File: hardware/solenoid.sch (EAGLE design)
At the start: 32 parts, among them U2 AP2204R

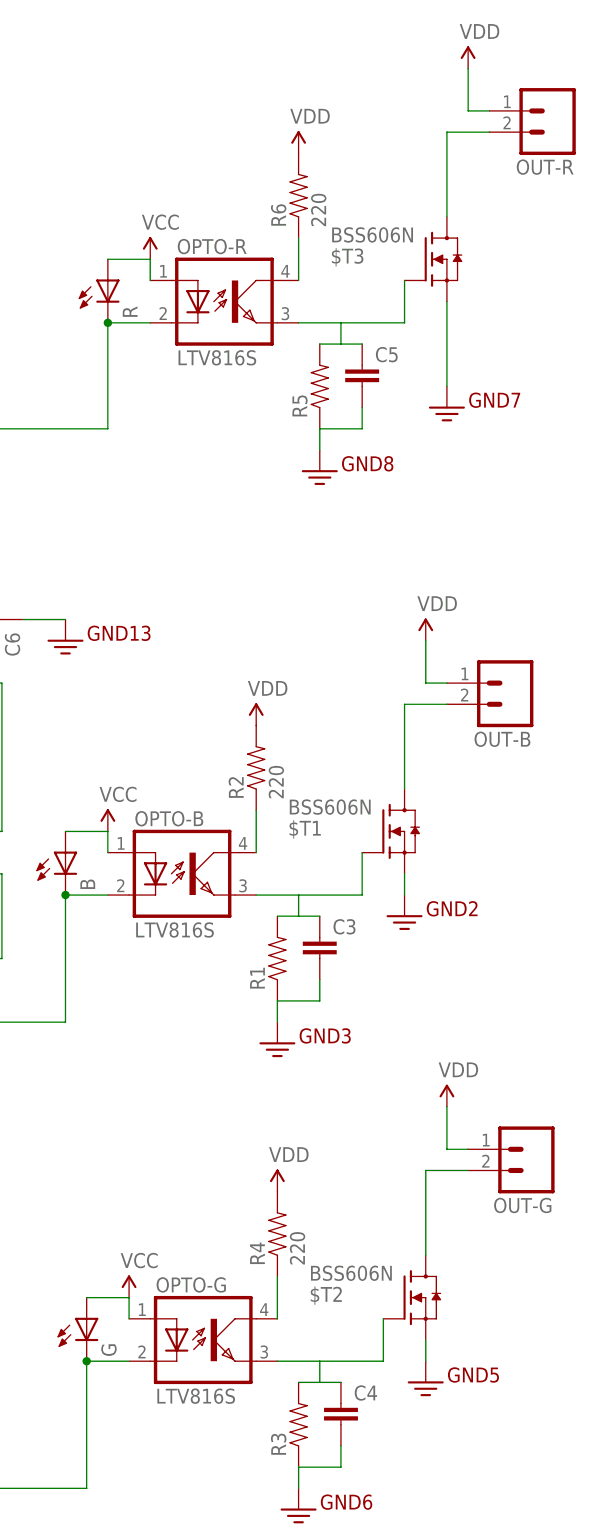
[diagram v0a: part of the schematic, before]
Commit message: Added protection diodes
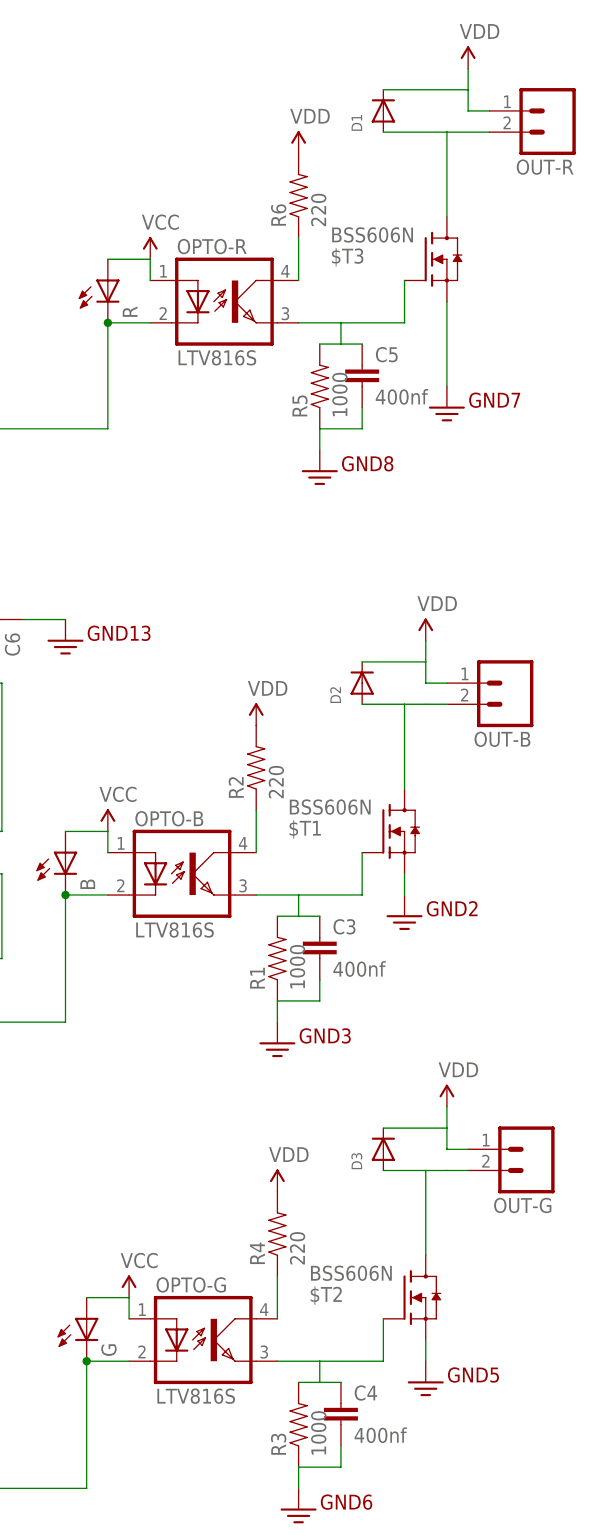
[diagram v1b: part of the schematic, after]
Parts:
- added D1, D2, D3: (no value), microbuilder:DIODESOD-123
- C3, C4, C5: value (none) -> 400nf
- R1, R3, R5: value (none) -> 1000
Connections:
- net N$12: now also D1.A
- net N$4: now also D2.A
- net N$8: now also D3.A
- net VDD: now also D1.C, D2.C, D3.C
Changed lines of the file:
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@@
 <part name="$T1" library="mishafarms" deviceset="BSS606N" device=""/>
 <part name="OPTO-B" library="optocoupler" deviceset="LTV816" device="S"/>
-<part name="R1" library="SparkFun-Passives" deviceset="RESISTOR" device="0805-RES"/>
+<part name="R1" library="SparkFun-Passives" deviceset="RESISTOR" device="0805-RES" value="1000"/>
 <part name="R2" library="SparkFun-Passives" deviceset="RESISTOR" device="0805-RES" value="220"/>
 <part name="GND1" library="SparkFun-Aesthetics" deviceset="GND2" device=""/>
@@
 <part name="C1" library="SparkFun-Capacitors" deviceset="CAP" device="0805" value="1uf"/>
 <part name="C2" library="SparkFun-Capacitors" deviceset="CAP" device="0805" value="2.2uf"/>
-<part name="C3" library="SparkFun-Capacitors" deviceset="CAP" device="0805"/>
+<part name="C3" library="SparkFun-Capacitors" deviceset="CAP" device="0805" value="400nf"/>
 <part name="$T2" library="mishafarms" deviceset="BSS606N" device=""/>
 <part name="OPTO-G" library="optocoupler" deviceset="LTV816" device="S"/>
-<part name="R3" library="SparkFun-Passives" deviceset="RESISTOR" device="0805-RES"/>
+<part name="R3" library="SparkFun-Passives" deviceset="RESISTOR" device="0805-RES" value="1000"/>
 <part name="R4" library="SparkFun-Passives" deviceset="RESISTOR" device="0805-RES" value="220"/>
 <part name="GND5" library="SparkFun-Aesthetics" deviceset="GND2" device=""/>
@@
 <part name="G" library="led" deviceset="LED" device="CHIPLED_0805"/>
 <part name="OUT-G" library="SparkFun-Connectors" deviceset="M02" device="PTH"/>
-<part name="C4" library="SparkFun-Capacitors" deviceset="CAP" device="0805"/>
+<part name="C4" library="SparkFun-Capacitors" deviceset="CAP" device="0805" value="400nf"/>
 <part name="$T3" library="mishafarms" deviceset="BSS606N" device=""/>
 <part name="OPTO-R" library="optocoupler" deviceset="LTV816" device="S"/>
-<part name="R5" library="SparkFun-Passives" deviceset="RESISTOR" device="0805-RES"/>
+<part name="R5" library="SparkFun-Passives" deviceset="RESISTOR" device="0805-RES" value="1000"/>
 <part name="R6" library="SparkFun-Passives" deviceset="RESISTOR" device="0805-RES" value="220"/>
 <part name="GND7" library="SparkFun-Aesthetics" deviceset="GND2" device=""/>
@@
 <part name="R" library="led" deviceset="LED" device="CHIPLED_0805"/>
 <part name="OUT-R" library="SparkFun-Connectors" deviceset="M02" device="PTH"/>
-<part name="C5" library="SparkFun-Capacitors" deviceset="CAP" device="0805"/>
+<part name="C5" library="SparkFun-Capacitors" deviceset="CAP" device="0805" value="400nf"/>
 <part name="IN" library="SparkFun-Connectors" deviceset="M03" device="1X03_NO_SILK"/>
 <part name="OUT" library="SparkFun-Connectors" deviceset="M03" device="1X03_NO_SILK"/>
@@
 <part name="GND13" library="SparkFun-Aesthetics" deviceset="GND2" device=""/>
 <part name="R8" library="SparkFun-Passives" deviceset="RESISTOR" device="0805-RES" value="100"/>
+<part name="D1" library="microbuilder" deviceset="DIODE" device="SOD-123"/>
+<part name="D2" library="microbuilder" deviceset="DIODE" device="SOD-123"/>
+<part name="D3" library="microbuilder" deviceset="DIODE" device="SOD-123"/>
 </parts>
 <sheets>
@@
 <instance part="GND13" gate="G$1" x="91.44" y="121.92"/>
 <instance part="R8" gate="G$1" x="78.74" y="132.08" rot="R270"/>
+<instance part="D1" gate="G$1" x="129.54" y="185.42" rot="R90"/>
+<instance part="D2" gate="G$1" x="127" y="116.84" rot="R90"/>
+<instance part="D3" gate="G$1" x="129.54" y="60.96" rot="R90"/>
 </instances>
 <busses>
@@
 <segment>
 <pinref part="SUPPLY3" gate="VDD" pin="VDD"/>
-<wire x1="134.62" y1="121.92" x2="134.62" y2="116.84" width="0.1524" layer="91"/>
+<wire x1="134.62" y1="121.92" x2="134.62" y2="119.38" width="0.1524" layer="91"/>
 <pinref part="OUT-B" gate="G$1" pin="1"/>
+<wire x1="134.62" y1="119.38" x2="134.62" y2="116.84" width="0.1524" layer="91"/>
 <wire x1="134.62" y1="116.84" x2="137.16" y2="116.84" width="0.1524" layer="91"/>
+<pinref part="D2" gate="G$1" pin="C"/>
+<wire x1="127" y1="119.38" x2="134.62" y2="119.38" width="0.1524" layer="91"/>
 </segment>
 <segment>
@@
 <segment>
 <pinref part="SUPPLY9" gate="VDD" pin="VDD"/>
-<wire x1="137.16" y1="66.04" x2="137.16" y2="60.96" width="0.1524" layer="91"/>
+<wire x1="137.16" y1="66.04" x2="137.16" y2="63.5" width="0.1524" layer="91"/>
 <pinref part="OUT-G" gate="G$1" pin="1"/>
+<wire x1="137.16" y1="63.5" x2="137.16" y2="60.96" width="0.1524" layer="91"/>
 <wire x1="137.16" y1="60.96" x2="139.7" y2="60.96" width="0.1524" layer="91"/>
+<pinref part="D3" gate="G$1" pin="C"/>
+<wire x1="129.54" y1="63.5" x2="137.16" y2="63.5" width="0.1524" layer="91"/>
 </segment>
 <segment>
@@
 <segment>
 <pinref part="SUPPLY12" gate="VDD" pin="VDD"/>
-<wire x1="139.7" y1="190.5" x2="139.7" y2="185.42" width="0.1524" layer="91"/>
+<wire x1="139.7" y1="190.5" x2="139.7" y2="187.96" width="0.1524" layer="91"/>
 <pinref part="OUT-R" gate="G$1" pin="1"/>
+<wire x1="139.7" y1="187.96" x2="139.7" y2="185.42" width="0.1524" layer="91"/>
 <wire x1="139.7" y1="185.42" x2="142.24" y2="185.42" width="0.1524" layer="91"/>
+<pinref part="D1" gate="G$1" pin="C"/>
+<wire x1="129.54" y1="187.96" x2="139.7" y2="187.96" width="0.1524" layer="91"/>
 </segment>
 <segment>
@@
 <segment>
 <pinref part="OUT-B" gate="G$1" pin="2"/>
-<wire x1="137.16" y1="114.3" x2="132.08" y2="114.3" width="0.1524" layer="91"/>
+<wire x1="137.16" y1="114.3" x2="134.62" y2="114.3" width="0.1524" layer="91"/>
 <pinref part="$T1" gate="G$1" pin="D"/>
+<wire x1="134.62" y1="114.3" x2="132.08" y2="114.3" width="0.1524" layer="91"/>
 <wire x1="132.08" y1="114.3" x2="132.08" y2="104.14" width="0.1524" layer="91"/>
+<pinref part="D2" gate="G$1" pin="A"/>
+<wire x1="127" y1="114.3" x2="132.08" y2="114.3" width="0.1524" layer="91"/>
 </segment>
 </net>
@@
 <segment>
 <pinref part="OUT-G" gate="G$1" pin="2"/>
-<wire x1="139.7" y1="58.42" x2="134.62" y2="58.42" width="0.1524" layer="91"/>
+<wire x1="139.7" y1="58.42" x2="137.16" y2="58.42" width="0.1524" layer="91"/>
 <pinref part="$T2" gate="G$1" pin="D"/>
+<wire x1="137.16" y1="58.42" x2="134.62" y2="58.42" width="0.1524" layer="91"/>
 <wire x1="134.62" y1="58.42" x2="134.62" y2="48.26" width="0.1524" layer="91"/>
+<pinref part="D3" gate="G$1" pin="A"/>
+<wire x1="129.54" y1="58.42" x2="134.62" y2="58.42" width="0.1524" layer="91"/>
 </segment>
 </net>
@@
 <pinref part="$T3" gate="G$1" pin="D"/>
 <wire x1="137.16" y1="182.88" x2="137.16" y2="172.72" width="0.1524" layer="91"/>
-</segment>
-</net>
+<pinref part="D1" gate="G$1" pin="A"/>
+<wire x1="129.54" y1="182.88" x2="137.16" y2="182.88" width="0.1524" layer="91"/>
+</segment>
+</net>

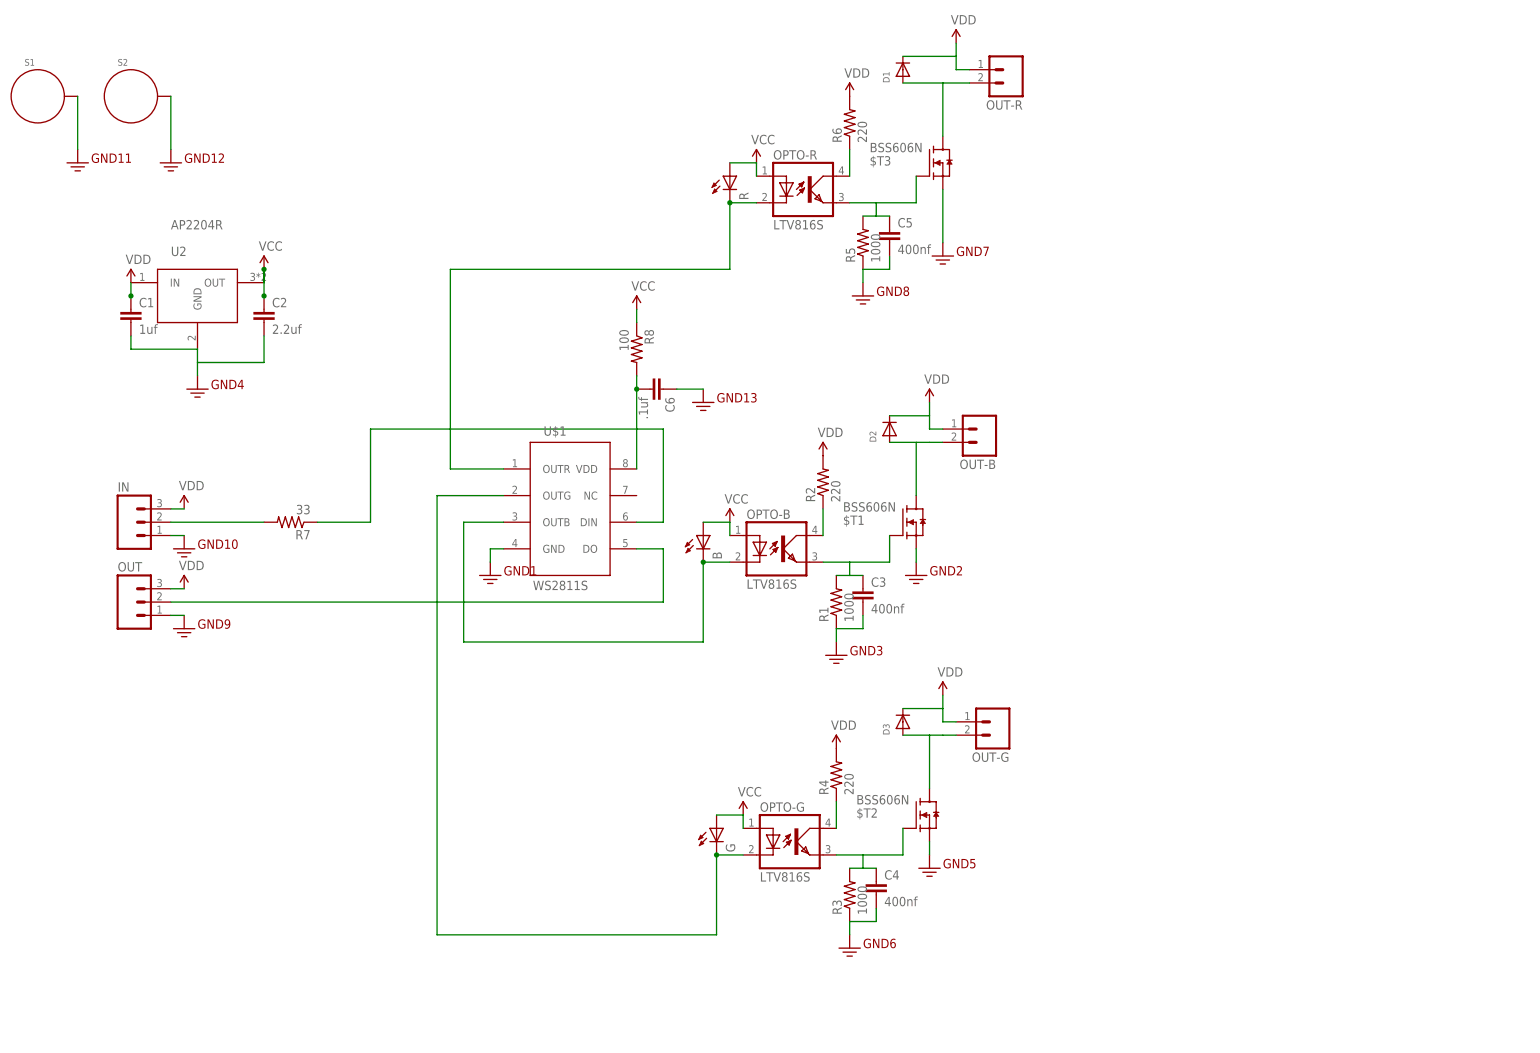
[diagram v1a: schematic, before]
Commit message: Changed to TSDs instead of flyback diodes and increased the solder holw sizes
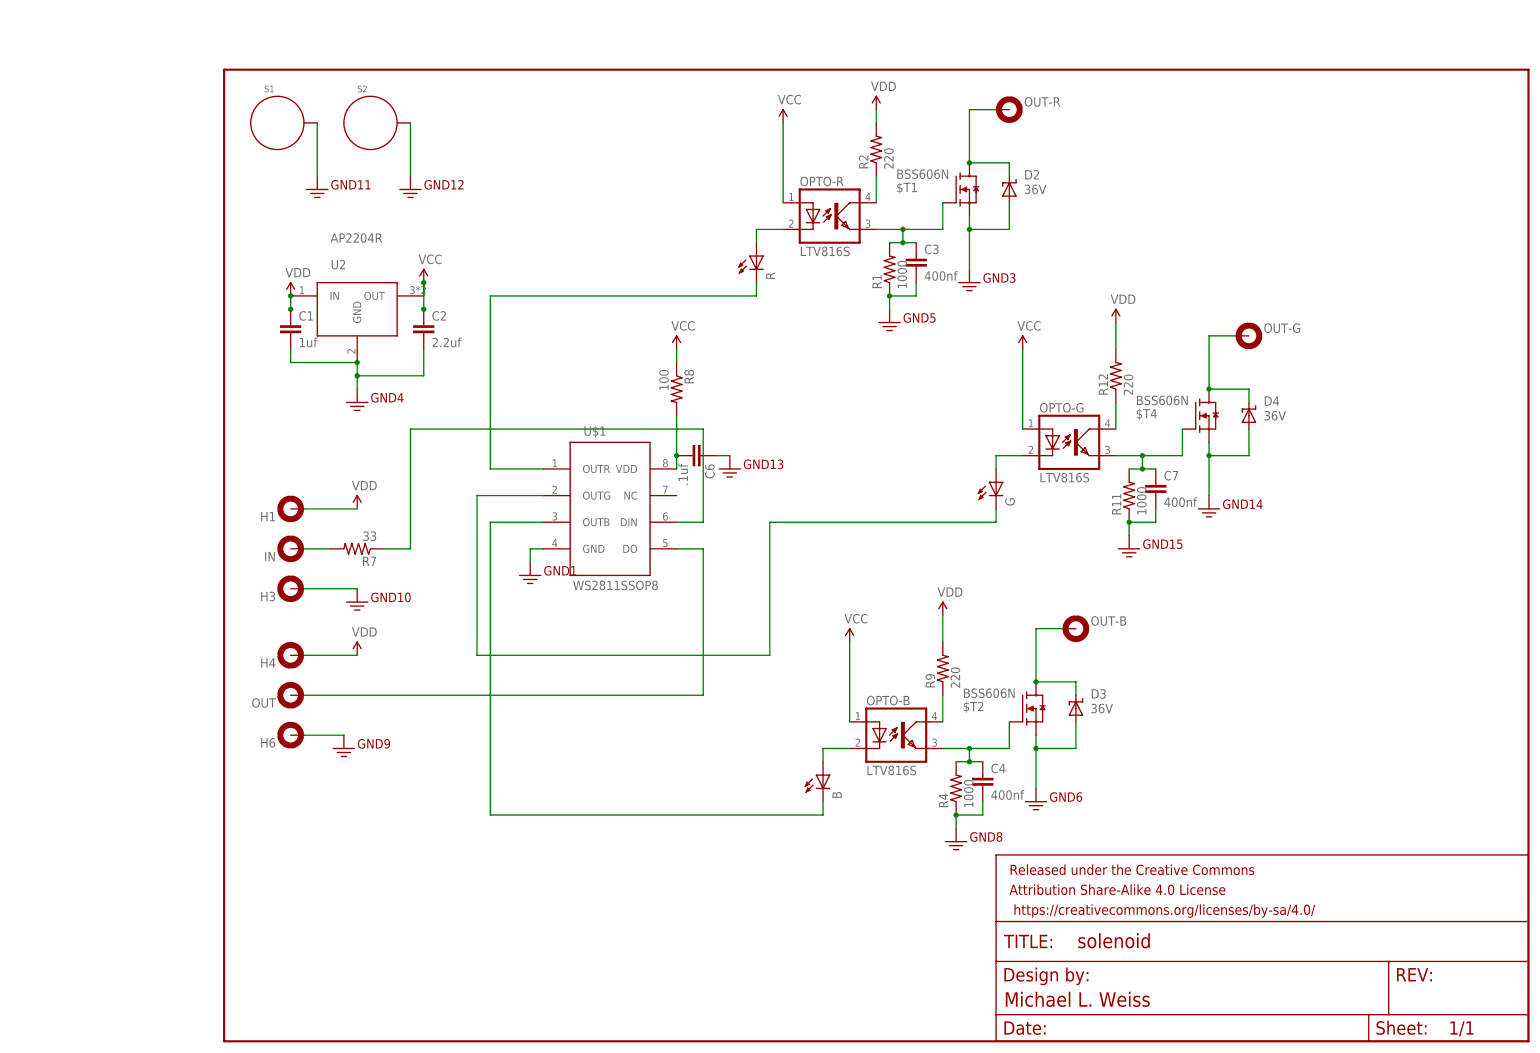
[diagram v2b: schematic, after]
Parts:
- removed $T3: BSS606N, mishafarms:BSS606N
- removed C5: 400nf, SparkFun-Capacitors:CAP0805
- removed D1: (no value), microbuilder:DIODESOD-123
- removed R3, R5: 1000, SparkFun-Passives:RESISTOR0805-RES
- removed R6: 220, SparkFun-Passives:RESISTOR0805-RES
- added $T4: BSS606N, mishafarms:BSS606N
- added C7: 400nf, SparkFun-Capacitors:CAP0805
- added D4: 36V, mishafarms:SUPPRESSOR-SMBJ
- added FRAME1: FRAME-LETTERNO_PACKAGE, SparkFun-Aesthetics:FRAME-LETTERNO_PACKAGE
- added H1, H3, H4, H6: MOUNT-PAD-ROUND2.8, holes:MOUNT-PAD-ROUND2.8
- added R11: 1000, SparkFun-Passives:RESISTOR0805-RES
- added R12, R9: 220, SparkFun-Passives:RESISTOR0805-RES
- D2, D3: value (none) -> 36V; device microbuilder:DIODESOD-123 -> mishafarms:SUPPRESSOR-SMBJ
- IN, OUT: value (none) -> MOUNT-PAD-ROUND2.8; device SparkFun-Connectors:M031X03_NO_SILK -> holes:MOUNT-PAD-ROUND2.8
- OUT-B, OUT-G, OUT-R: value (none) -> MOUNT-PAD-ROUND2.8; device SparkFun-Connectors:M02PTH -> holes:MOUNT-PAD-ROUND2.8
- R4: value 220 -> 1000
- U$1: value WS2811S -> WS2811SSOP8; device mishafarms:WS2811S -> mishafarms:WS2811SSOP8
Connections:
- removed net N$10: $T3.G, C5.1, OPTO-R.EMIT, R5.2
- removed net N$11: OPTO-R.COL, R6.1
- removed net N$14: OUT.2, U$1.DO
- removed net N$2: $T1.G, C3.1, OPTO-B.EMIT, R1.2
- removed net N$3: OPTO-B.COL, R2.1
- removed net N$30: IN.2, R7.2
- removed net N$4: $T1.D, D2.A, OUT-B.2
- new net IN: IN.MOUNT, R7.2
- new net N$15: OPTO-B.COL, R9.1
- new net N$16: B.A, OPTO-B.C
- new net N$19: $T4.G, C7.1, OPTO-G.EMIT, R11.2
- new net N$20: OPTO-G.COL, R12.1
- new net N$21: G.A, OPTO-G.C
- new net OUT: OUT.MOUNT, U$1.DO
- new net OUT-B: $T2.D, D3.C, OUT-B.MOUNT
- new net OUT-G: $T4.D, D4.C, OUT-G.MOUNT
- new net OUT-R: $T1.D, D2.C, OUT-R.MOUNT
- net GND: now also $T4.S, C7.2, D2.A, D3.A, D4.A, H3.MOUNT, H6.MOUNT, R11.1, R4.1; no longer $T3.S, C5.2, IN.1, OUT.1, R3.1, R5.1
- net N$1: no longer OPTO-B.C
- net N$12: now also $T2.G, C4.1, OPTO-B.EMIT, R4.2; no longer $T3.D, D1.A, OUT-R.2
- net N$5: no longer OPTO-G.C
- net N$6: now also $T1.G, C3.1, OPTO-R.EMIT, R1.2; no longer $T2.G, C4.1, OPTO-G.EMIT, R3.2
- net N$7: now also OPTO-R.COL, R2.1; no longer OPTO-G.COL, R4.1
- net N$8: now also OPTO-R.C, R.A; no longer $T2.D, D3.A, OUT-G.2
- net N$9: no longer OPTO-R.C
- net VCC: no longer B.A, G.A, R.A
- net VDD: now also H1.MOUNT, H4.MOUNT, R12.2, R9.2; no longer D1.C, D2.C, D3.C, IN.3, OUT-B.1, OUT-G.1, OUT-R.1, OUT.3, R4.2, R6.2
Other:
- moved on the sheet: $T1, $T2, B, C1, C2, C3, C4, C6, G, OPTO-B, OPTO-G, OPTO-R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
